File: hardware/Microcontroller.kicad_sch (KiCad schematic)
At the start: 34 parts, among them J11 Conn_01x08, J6 CON4, SW1 SW_Push, SW2 SW_Push, U1 W25Q128JVS, U3 RP2350_60QFN, Y1 ABM8-272-T3

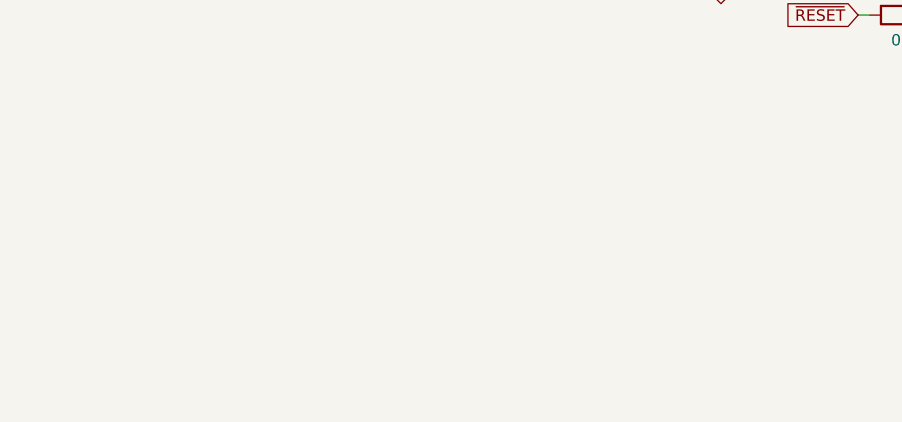
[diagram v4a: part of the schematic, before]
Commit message: All components placed on board and most 3D shapes are present
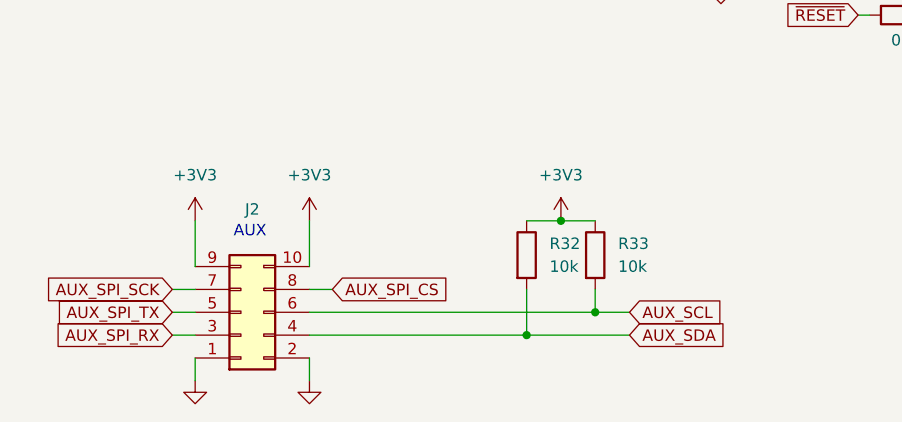
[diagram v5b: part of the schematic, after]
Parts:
- added J2: CON10, Connector_PinHeader_2.54mm:PinHeader_2x05_P2.54mm_Vertical, symbol Connector_Generic:Conn_02x05_Odd_Even
- added R32, R33: 10k, Resistor_SMD:R_0603_1608Metric, symbol Device:R
- L1: footprint RP2350_60QFN_minimal:L_pol_2016 -> BidirectionalSupply:L_pol_2016
- U3: footprint RP2350_60QFN_minimal:RP2350-QFN-60-1EP_7x7_P0.4mm_EP3.4x3.4mm_ThermalVias -> BidirectionalSupply:RP2350-QFN-60-1EP_7x7_P0.4mm_EP3.4x3.4mm_ThermalVias
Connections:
- net +3V3: now also J2.10 (Pin_10), J2.9 (Pin_9), R32.1, R33.1
- net AUX_SCL: now also J2.6 (Pin_6), R33.2
- net AUX_SDA: now also J2.4 (Pin_4), R32.2
- net AUX_SPI_CS: now also J2.8 (Pin_8)
- net AUX_SPI_RX: now also J2.3 (Pin_3)
- net AUX_SPI_SCK: now also J2.7 (Pin_7)
- net AUX_SPI_TX: now also J2.5 (Pin_5)
- net GND: now also J2.1 (Pin_1), J2.2 (Pin_2)
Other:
- note added: "AUX"

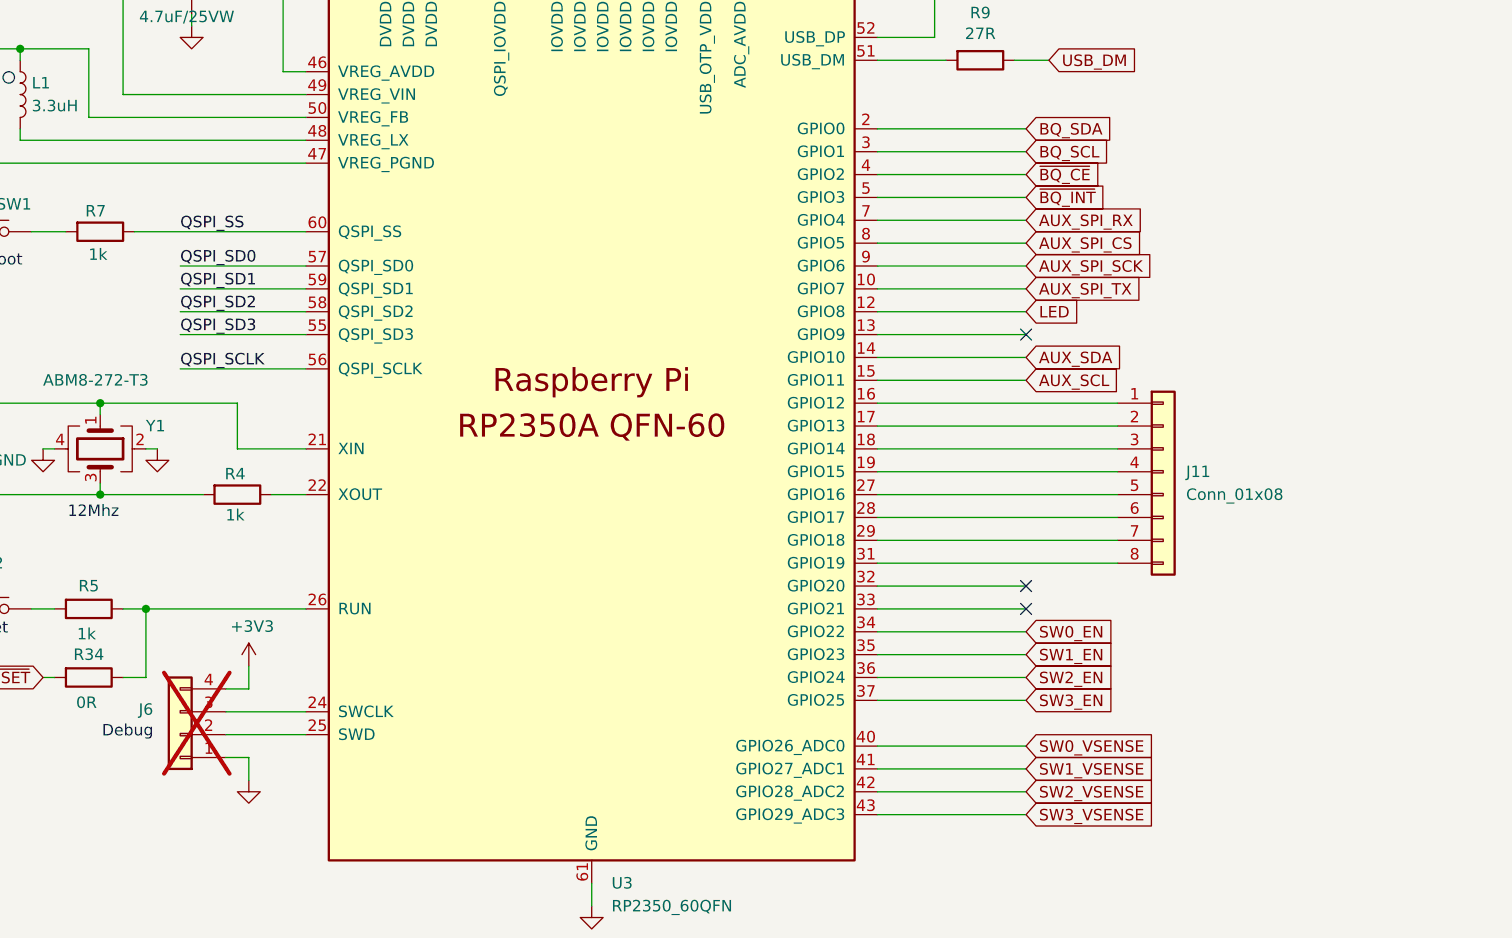
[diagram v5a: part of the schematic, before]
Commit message: - Routed board with all fixable DRC errors and warnings fixed
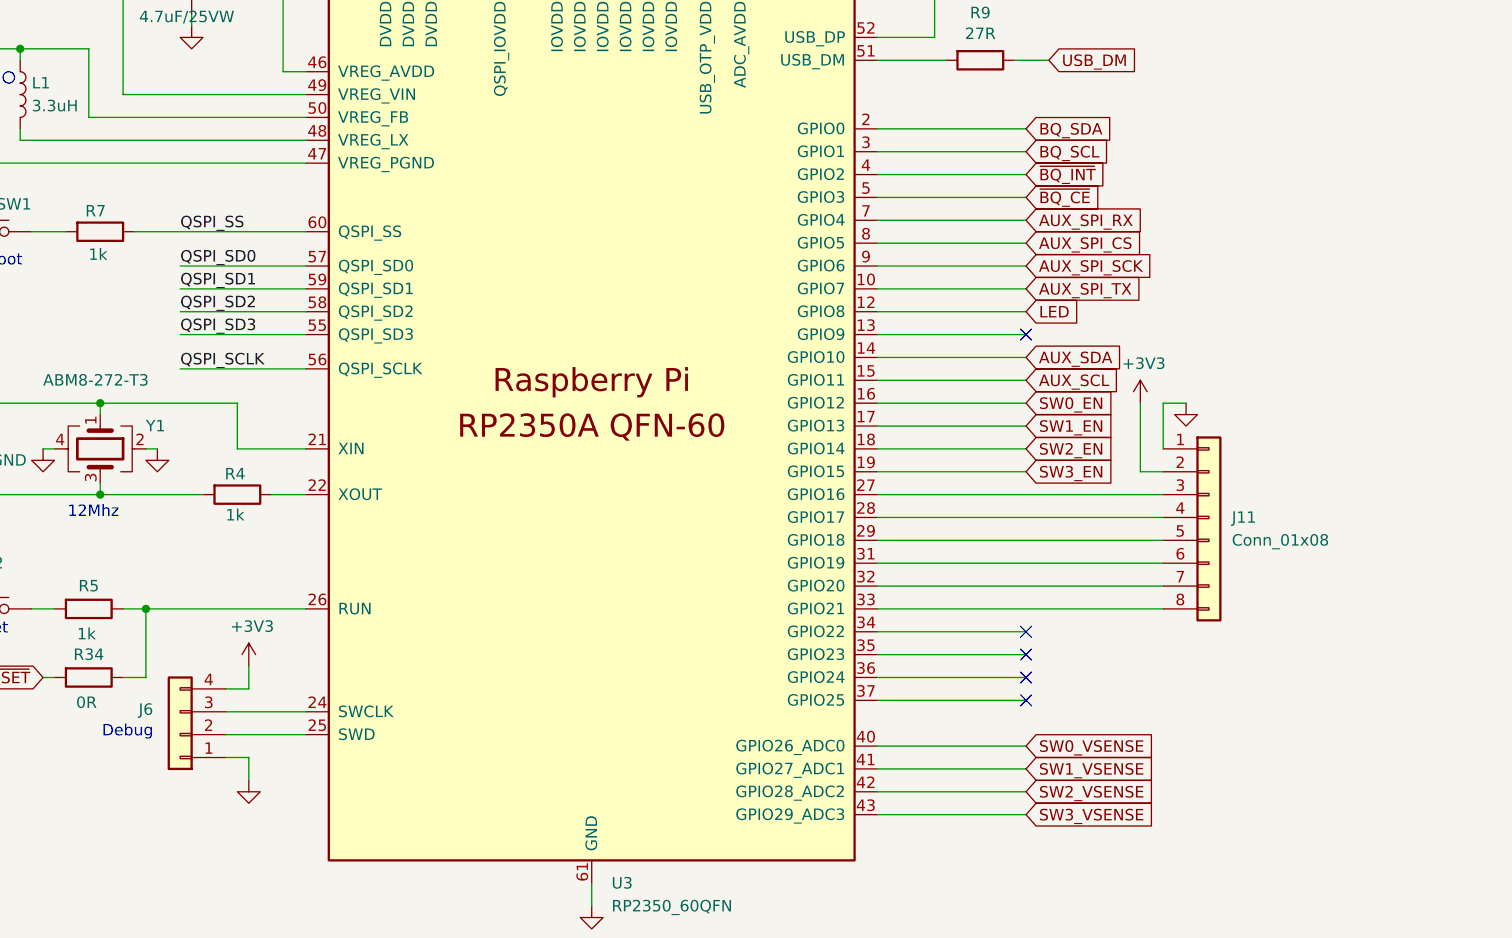
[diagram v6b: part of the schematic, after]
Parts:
- C1, C2: footprint Capacitor_SMD:C_0402_1005Metric -> BidirectionalSupply:C_0402_DRC
- J6: now fitted
- Y1: footprint Crystal:Crystal_SMD_3225-4Pin_3.2x2.5mm -> BidirectionalSupply:Crystal_SMD_3225-4Pin_DRC
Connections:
- net +3V3: now also J11.2 (Pin_2)
- net GND: now also J11.1 (Pin_1)
- net SW0_EN: now also U3.16 (GPIO12); no longer U3.34 (GPIO22)
- net SW1_EN: now also U3.17 (GPIO13); no longer U3.35 (GPIO23)
- net SW2_EN: now also U3.18 (GPIO14); no longer U3.36 (GPIO24)
- net SW3_EN: now also U3.19 (GPIO15); no longer U3.37 (GPIO25)
- net ~{BQ_CE}: now also U3.5 (GPIO3); no longer U3.4 (GPIO2)
- net ~{BQ_INT}: now also U3.4 (GPIO2); no longer U3.5 (GPIO3)
- net at J11.3 (Pin_3): now also U3.27 (GPIO16); no longer U3.18 (GPIO14)
- net at J11.4 (Pin_4): now also U3.28 (GPIO17); no longer U3.19 (GPIO15)
- net at J11.5 (Pin_5): now also U3.29 (GPIO18); no longer U3.27 (GPIO16)
- net at J11.6 (Pin_6): now also U3.31 (GPIO19); no longer U3.28 (GPIO17)
- net at J11.7 (Pin_7): now also U3.32 (GPIO20); no longer U3.29 (GPIO18)
- net at J11.8 (Pin_8): now also U3.33 (GPIO21); no longer U3.31 (GPIO19)
- no-connect marks 3 -> 5
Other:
- moved on the sheet: J11
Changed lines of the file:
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@@
 	)
 	(no_connect
-		(at 232.41 124.46)
+		(at 232.41 129.54)
 	)
 	(no_connect
-		(at 232.41 96.52)
+		(at 232.41 134.62)
+	)
+	(no_connect
+		(at 232.41 132.08)
+	)
+	(no_connect
+		(at 232.41 137.16)
 	)
 	(no_connect
-		(at 232.41 127)
+		(at 232.41 96.52)
 	)
 	(wire
@@
 	(wire
 		(pts
-			(xy 215.9 119.38) (xy 242.57 119.38)
+			(xy 215.9 119.38) (xy 247.65 119.38)
 		)
 		(stroke
@@
 	(wire
 		(pts
-			(xy 215.9 116.84) (xy 242.57 116.84)
+			(xy 215.9 116.84) (xy 247.65 116.84)
 		)
 		(stroke
@@
 	(wire
 		(pts
-			(xy 215.9 109.22) (xy 242.57 109.22)
+			(xy 215.9 109.22) (xy 232.41 109.22)
 		)
 		(stroke
@@
 	(wire
 		(pts
-			(xy 215.9 104.14) (xy 242.57 104.14)
+			(xy 215.9 104.14) (xy 232.41 104.14)
 		)
 		(stroke
@@
 	(wire
 		(pts
-			(xy 215.9 114.3) (xy 242.57 114.3)
+			(xy 215.9 114.3) (xy 247.65 114.3)
 		)
 		(stroke
@@
 	(wire
 		(pts
-			(xy 215.9 124.46) (xy 232.41 124.46)
+			(xy 215.9 124.46) (xy 247.65 124.46)
 		)
 		(stroke
@@
 	(wire
 		(pts
+			(xy 245.11 104.14) (xy 245.11 111.76)
+		)
+		(stroke
+			(width 0)
+			(type default)
+		)
+	)
+	(wire
+		(pts
 			(xy 140.97 33.02) (xy 152.4 33.02)
 		)
@@
 	(wire
 		(pts
+			(xy 245.11 111.76) (xy 247.65 111.76)
+		)
+		(stroke
+			(width 0)
+			(type default)
+		)
+	)
+	(wire
+		(pts
 			(xy 232.41 22.86) (xy 243.84 22.86)
 		)
@@
 	(wire
 		(pts
-			(xy 215.9 121.92) (xy 242.57 121.92)
+			(xy 215.9 121.92) (xy 247.65 121.92)
 		)
 		(stroke
@@
 	(wire
 		(pts
-			(xy 215.9 127) (xy 232.41 127)
+			(xy 215.9 127) (xy 247.65 127)
 		)
 		(stroke
@@
 	(wire
 		(pts
+			(xy 247.65 104.14) (xy 247.65 109.22)
+		)
+		(stroke
+			(width 0)
+			(type default)
+		)
+	)
+	(wire
+		(pts
 			(xy 266.7 34.29) (xy 278.13 34.29)
 		)
@@
 	(wire
 		(pts
-			(xy 215.9 106.68) (xy 242.57 106.68)
+			(xy 215.9 106.68) (xy 232.41 106.68)
 		)
 		(stroke
@@
 	(wire
 		(pts
+			(xy 250.19 104.14) (xy 247.65 104.14)
+		)
+		(stroke
+			(width 0)
+			(type default)
+		)
+	)
+	(wire
+		(pts
 			(xy 215.9 99.06) (xy 232.41 99.06)
 		)
@@
 	(wire
 		(pts
-			(xy 215.9 111.76) (xy 242.57 111.76)
+			(xy 215.9 111.76) (xy 232.41 111.76)
 		)
 		(stroke
@@
 	(global_label "SW2_EN"
 		(shape input)
-		(at 232.41 134.62 0)
+		(at 232.41 109.22 0)
 		(fields_autoplaced yes)
 		(effects
@@
 		)
 		(property "Intersheetrefs" "${INTERSHEET_REFS}"
-			(at 242.7127 134.62 0)
+			(at 242.7127 109.22 0)
 			(effects
 				(font
@@
 	(global_label "~{BQ_CE}"
 		(shape input)
-		(at 232.41 78.74 0)
+		(at 232.41 81.28 0)
 		(fields_autoplaced yes)
 		(effects
@@
 		)
 		(property "Intersheetrefs" "${INTERSHEET_REFS}"
-			(at 241.3823 78.74 0)
+			(at 241.3823 81.28 0)
 			(effects
 				(font
@@
 	(global_label "~{BQ_INT}"
 		(shape input)
-		(at 232.41 81.28 0)
+		(at 232.41 78.74 0)
 		(fields_autoplaced yes)
 		(effects
@@
 		)
 		(property "Intersheetrefs" "${INTERSHEET_REFS}"
-			(at 241.8662 81.28 0)
+			(at 241.8662 78.74 0)
 			(effects
 				(font
@@
 	(global_label "SW3_EN"
 		(shape input)
-		(at 232.41 137.16 0)
+		(at 232.41 111.76 0)
 		(fields_autoplaced yes)
 		(effects
@@
 		)
 		(property "Intersheetrefs" "${INTERSHEET_REFS}"
-			(at 242.7127 137.16 0)
+			(at 242.7127 111.76 0)
 			(effects
 				(font
@@
 	(global_label "SW1_EN"
 		(shape input)
-		(at 232.41 132.08 0)
+		(at 232.41 106.68 0)
 		(fields_autoplaced yes)
 		(effects
@@
 		)
 		(property "Intersheetrefs" "${INTERSHEET_REFS}"
-			(at 242.7127 132.08 0)
+			(at 242.7127 106.68 0)
 			(effects
 				(font
@@
 	(global_label "SW0_EN"
 		(shape input)
-		(at 232.41 129.54 0)
+		(at 232.41 104.14 0)
 		(fields_autoplaced yes)
 		(effects
@@
 		)
 		(property "Intersheetrefs" "${INTERSHEET_REFS}"
-			(at 242.7127 129.54 0)
+			(at 242.7127 104.14 0)
 			(effects
 				(font
@@
 	)
 	(symbol
+		(lib_id "power:GND")
+		(at 250.19 104.14 0)
+		(unit 1)
+		(exclude_from_sim no)
+		(in_bom yes)
+		(on_board yes)
+		(dnp no)
+		(property "Reference" "#PWR0114"
+			(at 250.19 110.49 0)
+			(effects
+				(font
+					(size 1.27 1.27)
+				)
+				(hide yes)
+			)
+		)
+		(property "Value" "GND"
+			(at 250.317 108.5342 0)
+			(effects
+				(font
+					(size 1.27 1.27)
+				)
+				(hide yes)
+			)
+		)
+		(property "Footprint" ""
+			(at 250.19 104.14 0)
+			(effects
+				(font
+					(size 1.27 1.27)
+				)
+				(hide yes)
+			)
+		)
+		(property "Datasheet" ""
+			(at 250.19 104.14 0)
+			(effects
+				(font
+					(size 1.27 1.27)
+				)
+				(hide yes)
+			)
+		)
+		(property "Description" "Power symbol creates a global label with name \"GND\" , ground"
+			(at 250.19 104.14 0)
+			(effects
+				(font
+					(size 1.27 1.27)
+				)
+				(hide yes)
+			)
+		)
+		(pin "1"
+		)
+		(instances
+			(project "BidirectionalSupply"
+				(path "/e5771ea0-f106-4b1c-9531-189f5725062b/1c1be91e-b9b6-4767-b4a3-64867bdbc875"
+					(reference "#PWR0114")
+					(unit 1)
+				)
+			)
+		)
+	)
+	(symbol
 		(lib_id "power:+1V1")
 		(at 161.29 21.59 0)
@@
 			)
 		)
-		(property "Footprint" "Crystal:Crystal_SMD_3225-4Pin_3.2x2.5mm"
+		(property "Footprint" "BidirectionalSupply:Crystal_SMD_3225-4Pin_DRC"
 			(at 129.54 109.22 0)
 			(effects
@@
 			)
 		)
-		(property "Footprint" "Capacitor_SMD:C_0402_1005Metric"
+		(property "Footprint" "BidirectionalSupply:C_0402_DRC"
 			(at 110.49 115.2652 0)
 			(effects
@@
 		(in_bom yes)
 		(on_board yes)
-		(dnp yes)
+		(dnp no)
 		(property "Reference" "J6"
 			(at 134.62 138.176 0)
@@
 	)
 	(symbol
+		(lib_id "power:+3V3")
+		(at 245.11 104.14 0)
+		(unit 1)
+		(exclude_from_sim no)
+		(in_bom yes)
+		(on_board yes)
+		(dnp no)
+		(property "Reference" "#PWR0115"
+			(at 245.11 107.95 0)
+			(effects
+				(font
+					(size 1.27 1.27)
+				)
+				(hide yes)
+			)
+		)
+		(property "Value" "+3V3"
+			(at 245.491 99.7458 0)
+			(effects
+				(font
+					(size 1.27 1.27)
+				)
+			)
+		)
+		(property "Footprint" ""
+			(at 245.11 104.14 0)
+			(effects
+				(font
+					(size 1.27 1.27)
+				)
+				(hide yes)
+			)
+		)
+		(property "Datasheet" ""
+			(at 245.11 104.14 0)
+			(effects
+				(font
+					(size 1.27 1.27)
+				)
+				(hide yes)
+			)
+		)
+		(property "Description" "Power symbol creates a global label with name \"+3V3\""
+			(at 245.11 104.14 0)
+			(effects
+				(font
+					(size 1.27 1.27)
+				)
+				(hide yes)
+			)
+		)
+		(pin "1"
+		)
+		(instances
+			(project "BidirectionalSupply"
+				(path "/e5771ea0-f106-4b1c-9531-189f5725062b/1c1be91e-b9b6-4767-b4a3-64867bdbc875"
+					(reference "#PWR0115")
+					(unit 1)
+				)
+			)
+		)
+	)
+	(symbol
 		(lib_id "Device:R")
 		(at 128.27 134.62 270)
@@
 			)
 		)
-		(property "Footprint" "Capacitor_SMD:C_0402_1005Metric"
+		(property "Footprint" "BidirectionalSupply:C_0402_DRC"
 			(at 110.49 105.1052 0)
 			(effects
@@
 	(symbol
 		(lib_id "Connector_Generic:Conn_01x08")
-		(at 247.65 111.76 0)
+		(at 252.73 116.84 0)
 		(unit 1)
 		(exclude_from_sim no)
@@
 		(fields_autoplaced yes)
 		(property "Reference" "J11"
-			(at 250.19 111.7599 0)
+			(at 255.27 116.8399 0)
 			(effects
 				(font
@@
 		)
 		(property "Value" "Conn_01x08"
-			(at 250.19 114.2999 0)
+			(at 255.27 119.3799 0)
 			(effects
 				(font
@@
 		)
 		(property "Footprint" "Connector_PinHeader_2.54mm:PinHeader_1x08_P2.54mm_Vertical"
-			(at 247.65 111.76 0)
+			(at 252.73 116.84 0)
 			(effects
 				(font
@@
 		)
 		(property "Datasheet" "~"
-			(at 247.65 111.76 0)
+			(at 252.73 116.84 0)
 			(effects
 				(font
@@
 		)
 		(property "Description" "Generic connector, single row, 01x08, script generated (kicad-library-utils/schlib/autogen/connector/)"
-			(at 247.65 111.76 0)
+			(at 252.73 116.84 0)
 			(effects
 				(font
@@
 		)
 		(property "Mouser" ""
-			(at 247.65 111.76 0)
+			(at 252.73 116.84 0)
 			(effects
 				(font

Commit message: * Added the JLCPCB Fabrication Plugin into KiCad and use this for the exports * Fixed problem detected with capacitor footprint for C42, C43, C44, C50, C51, C52
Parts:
- C1, C2: LCSC Part (none) -> C1548
- C10, C6, C7, C9: LCSC Part (none) -> C1779
- C11, C12, C13, C14, C15, C16, C18, C19, C4, C8: LCSC Part (none) -> C1590
- C17: LCSC Part (none) -> C15850
- D15: LCSC Part (none) -> C2286
- L1: LCSC Part (none) -> C42411119
- R32, R33: LCSC Part (none) -> C25804
- R34: LCSC Part (none) -> C21189
- R4, R5, R58, R7: LCSC Part (none) -> C21190
- R6: LCSC Part (none) -> C23140
- R8, R9: LCSC Part (none) -> C25190
- SW1, SW2: LCSC Part (none) -> C720477
- U1: LCSC Part (none) -> C97521
- U3: LCSC Part (none) -> C42411118
- Y1: LCSC Part (none) -> C20625731
